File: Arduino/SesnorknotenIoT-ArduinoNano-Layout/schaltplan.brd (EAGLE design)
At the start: 68.2 x 69.8 mm, 10 parts

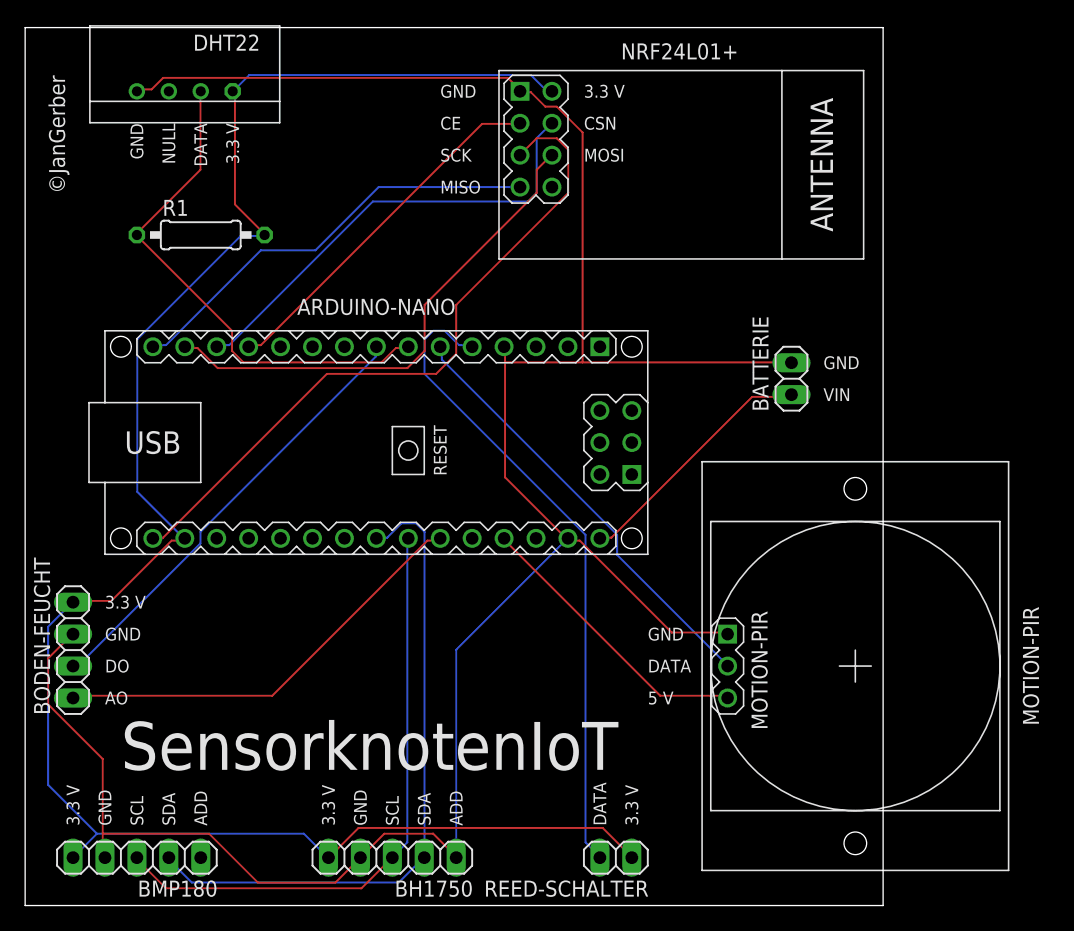
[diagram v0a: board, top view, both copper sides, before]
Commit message: Eagle +Reed Schalter +1-Wire +Schalter stromversorgung
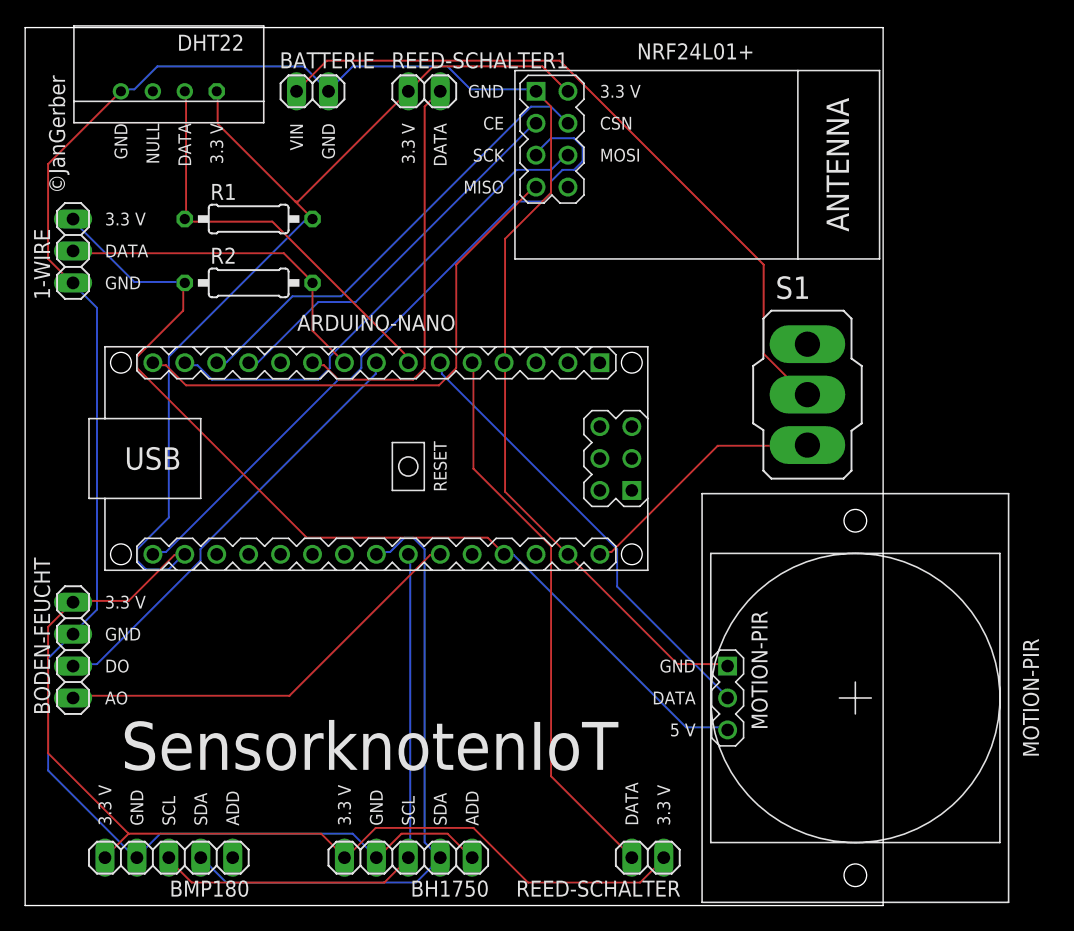
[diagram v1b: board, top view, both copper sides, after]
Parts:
- added 1-WIRE: (no value), pinhead:1X03
- added R2: 4k7, resistor:0207/10
- added REED-SCHALTER1: (no value), pinhead:1X02
- added S1: (no value), switch:320-916
- moved BATTERIE 44.4 mm to (22.9, 64.8), turned to 0 degrees
- moved R1 4.02 mm to (17.8, 54.6)
- moved BMP180 2.54 mm to (11.4, 3.81)
- moved MOTION-PIR 2.54 mm to (66.0, 16.5)
- moved REED-SCHALTER 2.54 mm to (49.5, 3.81)
- moved NRF24L01+ 1.27 mm to (53.3, 58.4)
- moved BH1750 1.27 mm to (30.5, 3.81)
- moved DHT22 1.27 mm to (11.4, 64.8)
- moved ARDUINO-NANO 1.27 mm to (27.9, 35.6)
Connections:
- new net N$5: BATTERIE.1, S1.2
- new net N$6: 1-WIRE.2, ARDUINO-NANO.J1.9, R2.2
- new net N$7: ARDUINO-NANO.J1.10, REED-SCHALTER1.2
- net 3.3V: now also REED-SCHALTER1.1
- net 5V: now also 1-WIRE.3, R2.1
- net GND: now also 1-WIRE.1
- net N$13: now also S1.3; no longer BATTERIE.1
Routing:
- net N$5: track 0.00 -> 57.0 mm
- net 5V: track 23.1 -> 78.3 mm
- net N$7: track 0.00 -> 32.5 mm
- net N$6: track 0.00 -> 27.6 mm
- net 3.3V: track 149.9 -> 160.2 mm
- net MISO: track 34.5 -> 42.6 mm
- net N$1: track 40.8 -> 33.1 mm
- net N$2: track 51.6 -> 44.6 mm
- net SCL: track 48.3 -> 45.1 mm
- net SDA: track 52.6 -> 50.5 mm
- net N$9: track 29.0 -> 30.7 mm
- net N$8: track 34.9 -> 36.1 mm
- net MOSI: track 40.1 -> 39.0 mm
- net SCK: track 54.9 -> 54.0 mm
- net GND: track 194.0 -> 193.1 mm
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
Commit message: Änderungen Sender Verschlüsselung und Encodierung
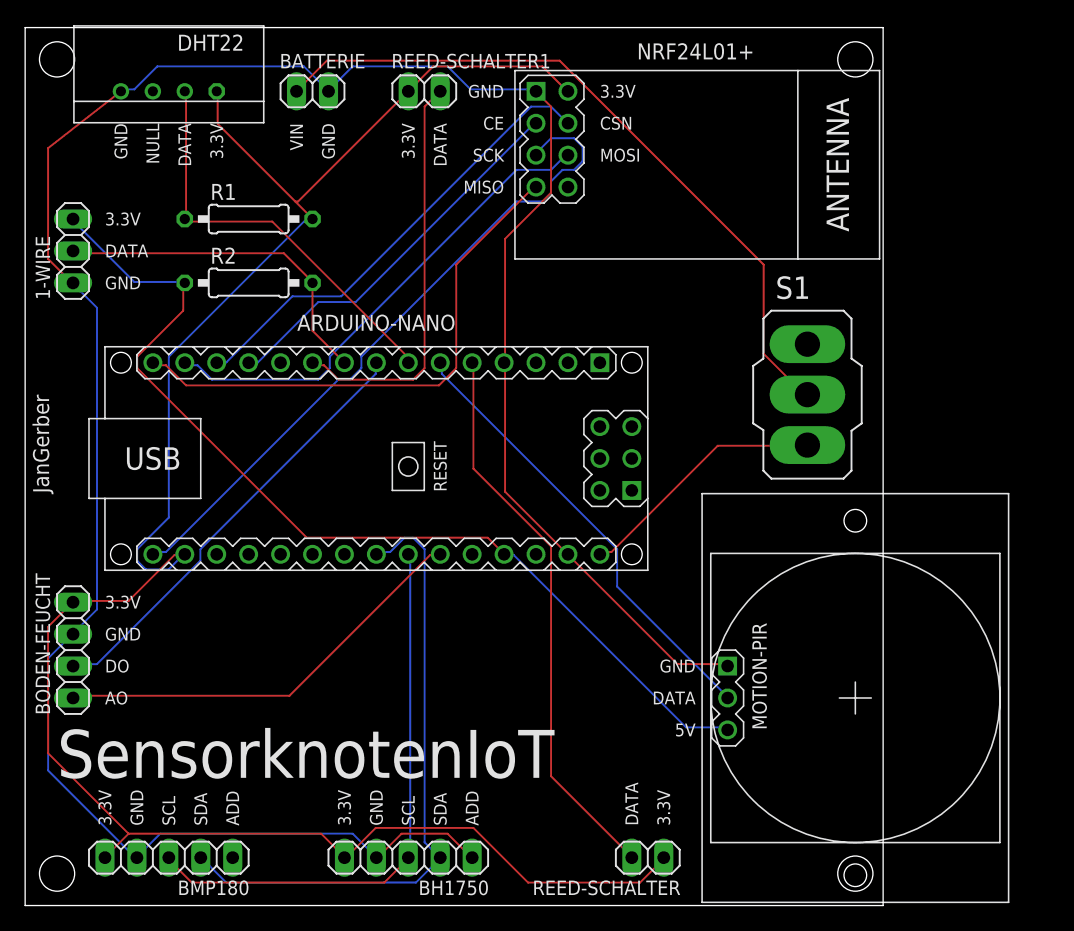
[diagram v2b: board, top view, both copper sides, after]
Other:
- board text added: "3.3V"
- board text added: "5V"
- board text added: "JanGerber"
- board text removed: "3.3 V"
- board text removed: "5 V"
- board text removed: "©JanGerber"
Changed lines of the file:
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@@
 <drawing>
 <settings>
-<setting alwaysvectorfont="no"/>
+<setting alwaysvectorfont="yes"/>
 <setting verticaltext="up"/>
 </settings>
@@
 <text x="53.34" y="19.05" size="1.016" layer="21" rot="R180" align="center-left">GND</text>
 <text x="53.34" y="16.51" size="1.016" layer="21" rot="R180" align="center-left">DATA</text>
-<text x="53.34" y="13.97" size="1.016" layer="21" rot="R180" align="center-left">5 V</text>
-<text x="50.8" y="6.35" size="1.016" layer="21" rot="R90" align="center-left">3.3 V</text>
-<text x="25.4" y="6.35" size="1.016" layer="21" rot="R90" align="center-left">3.3 V</text>
-<text x="6.35" y="6.35" size="1.016" layer="21" rot="R90" align="center-left">3.3 V</text>
-<text x="6.35" y="24.13" size="1.016" layer="21" align="center-left">3.3 V</text>
+<text x="53.34" y="13.97" size="1.016" layer="21" rot="R180" align="center-left">5V</text>
+<text x="50.8" y="6.35" size="1.016" layer="21" rot="R90" align="center-left">3.3V</text>
+<text x="25.4" y="6.35" size="1.016" layer="21" rot="R90" align="center-left">3.3V</text>
+<text x="6.35" y="6.35" size="1.016" layer="21" rot="R90" align="center-left">3.3V</text>
+<text x="6.35" y="24.13" size="1.016" layer="21" align="center-left">3.3V</text>
 <text x="27.94" y="6.35" size="1.016" layer="21" rot="R90" align="center-left">GND</text>
 <text x="8.89" y="6.35" size="1.016" layer="21" rot="R90" align="center-left">GND</text>
@@
 <text x="7.62" y="62.23" size="1.016" layer="21" rot="R270" align="center-left">GND</text>
 <text x="12.7" y="62.23" size="1.016" layer="21" rot="R270" align="center-left">DATA</text>
-<text x="15.24" y="62.23" size="1.016" layer="21" rot="R270" align="center-left">3.3 V</text>
+<text x="15.24" y="62.23" size="1.016" layer="21" rot="R270" align="center-left">3.3V</text>
 <text x="10.16" y="62.23" size="1.016" layer="21" rot="R270" align="center-left">NULL</text>
-<text x="45.72" y="64.77" size="1.016" layer="21" align="center-left">3.3 V</text>
+<text x="45.72" y="64.77" size="1.016" layer="21" align="center-left">3.3V</text>
 <text x="38.1" y="64.77" size="1.016" layer="21" rot="R180" align="center-left">GND</text>
 <text x="38.1" y="59.69" size="1.016" layer="21" rot="R180" align="center-left">SCK</text>
@@
 <text x="38.1" y="62.23" size="1.016" layer="21" rot="R180" align="center-left">CE</text>
 <text x="45.72" y="62.23" size="1.016" layer="21" align="center-left">CSN</text>
-<text x="58.42" y="13.97" size="1.27" layer="21" rot="R90" align="center-left">MOTION-PIR</text>
+<text x="58.42" y="13.97" size="1.143" layer="21" font="vector" rot="R90" align="center-left">MOTION-PIR</text>
 <text x="21.59" y="62.23" size="1.016" layer="21" rot="R270" align="center-left">VIN</text>
 <text x="24.13" y="62.23" size="1.016" layer="21" rot="R270" align="center-left">GND</text>
-<text x="7.62" y="12.7" size="3.81" layer="21" ratio="31" align="center-left">SensorknotenIoT</text>
-<text x="46.99" y="12.7" size="3.81" layer="22" ratio="31" rot="MR0" align="center-left">SensorknotenIoT</text>
-<text x="64.77" y="2.54" size="1.6764" layer="22" ratio="31" rot="MR0" align="center-left">©JanGerber</text>
-<text x="2.54" y="66.04" size="1.27" layer="21" ratio="31" rot="R270" align="center-left">©JanGerber</text>
-<text x="30.48" y="62.23" size="1.016" layer="21" rot="R270" align="center-left">3.3 V</text>
+<text x="31.75" y="1.27" size="1.6764" layer="22" font="vector" ratio="12" rot="MR0" align="center-left">JanGerber</text>
+<text x="1.27" y="40.64" size="1.27" layer="21" font="vector" ratio="11" rot="R270" align="center-left">JanGerber</text>
+<text x="30.48" y="62.23" size="1.016" layer="21" rot="R270" align="center-left">3.3V</text>
 <text x="33.02" y="62.23" size="1.016" layer="21" rot="R270" align="center-left">DATA</text>
 <text x="6.35" y="49.53" size="1.016" layer="21" align="center-left">GND</text>
-<text x="6.35" y="54.61" size="1.016" layer="21" align="center-left">3.3 V</text>
+<text x="6.35" y="54.61" size="1.016" layer="21" align="center-left">3.3V</text>
 <text x="6.35" y="52.07" size="1.016" layer="21" align="center-left">DATA</text>
+<text x="2.54" y="10.16" size="3.81" layer="25" font="vector" ratio="14">SensorknotenIoT</text>
+<text x="50.8" y="10.16" size="3.81" layer="26" font="vector" ratio="14" rot="MR0">SensorknotenIoT</text>
+<hole x="2.54" y="2.54" drill="2.8"/>
+<hole x="66.04" y="2.54" drill="2.8"/>
+<hole x="66.04" y="67.31" drill="2.8"/>
+<hole x="2.54" y="67.31" drill="2.8"/>
 </plain>
 <attributes>
@@
 </autorouter>
 <elements>
-<element name="BATTERIE" library="pinhead" package="1X02" value="" x="22.86" y="64.77"/>
-<element name="BMP180" library="pinhead" package="1X05" value="" x="11.43" y="3.81" rot="R180"/>
+<element name="BATTERIE" library="pinhead" package="1X02" value="" x="22.86" y="64.77" smashed="yes">
+<attribute name="NAME" x="20.2438" y="66.5988" size="1.143" layer="25" font="vector" ratio="10"/>
+<attribute name="VALUE" x="20.32" y="61.595" size="1.27" layer="27"/>
+</element>
+<element name="BMP180" library="pinhead" package="1X05" value="" x="11.43" y="3.81" smashed="yes" rot="R180">
+<attribute name="NAME" x="17.8562" y="1.9812" size="1.143" layer="25" font="vector" ratio="10" rot="R180"/>
+<attribute name="VALUE" x="17.78" y="6.985" size="1.27" layer="27" rot="R180"/>
+</element>
 <element name="ARDUINO-NANO" library="diy-modules" package="ARDUINO-NANO-3.0#ISP" value="" x="27.94" y="35.56"/>
 <element name="NRF24L01+" library="diy-modules" package="WIRELESS-NRF24L01" value="" x="53.34" y="58.42"/>
 <element name="R1" library="resistor" package="0207/10" value="10k" x="17.78" y="54.61"/>
-<element name="MOTION-PIR" library="diy-modules" package="MOTION-PIR-DYP-ME003" value="" x="66.04" y="16.51" rot="R270"/>
+<element name="MOTION-PIR" library="diy-modules" package="MOTION-PIR-DYP-ME003" value="" x="66.04" y="16.51" smashed="yes" rot="R270">
+<attribute name="VALUE" x="52.705" y="16.51" size="1.27" layer="27" rot="R270" align="top-center"/>
+</element>
 <element name="DHT22" library="RHT03_DHT-22_AM2302" package="RHT03_DHT-22" value="" x="11.43" y="64.77" rot="R180">
 <attribute name="PROD_ID" value="SEN-10167" x="11.43" y="64.77" size="1.778" layer="27" rot="R180" display="off"/>
 </element>
-<element name="BH1750" library="pinhead" package="1X05" value="" x="30.48" y="3.81" rot="R180"/>
-<element name="REED-SCHALTER" library="pinhead" package="1X02" value="" x="49.53" y="3.81" rot="R180"/>
-<element name="BODEN-FEUCHT" library="pinhead" package="1X04" value="" x="3.81" y="20.32" rot="R90"/>
-<element name="1-WIRE" library="pinhead" package="1X03" value="" x="3.81" y="52.07" rot="R90"/>
+<element name="BH1750" library="pinhead" package="1X05" value="" x="30.48" y="3.81" smashed="yes" rot="R180">
+<attribute name="NAME" x="36.9062" y="1.9812" size="1.143" layer="25" font="vector" ratio="10" rot="R180"/>
+<attribute name="VALUE" x="36.83" y="6.985" size="1.27" layer="27" rot="R180"/>
+</element>
+<element name="REED-SCHALTER" library="pinhead" package="1X02" value="" x="49.53" y="3.81" smashed="yes" rot="R180">
+<attribute name="NAME" x="52.1462" y="1.9812" size="1.143" layer="25" font="vector" ratio="10" rot="R180"/>
+<attribute name="VALUE" x="52.07" y="6.985" size="1.27" layer="27" rot="R180"/>
+</element>
+<element name="BODEN-FEUCHT" library="pinhead" package="1X04" value="" x="3.81" y="20.32" smashed="yes" rot="R90">
+<attribute name="NAME" x="1.9812" y="15.1638" size="1.143" layer="25" font="vector" ratio="10" rot="R90"/>
+<attribute name="VALUE" x="6.985" y="15.24" size="1.27" layer="27" rot="R90"/>
+</element>
+<element name="1-WIRE" library="pinhead" package="1X03" value="" x="3.81" y="52.07" smashed="yes" rot="R90">
+<attribute name="NAME" x="1.9812" y="48.1838" size="1.143" layer="25" font="vector" ratio="10" rot="R90"/>
+<attribute name="VALUE" x="6.985" y="48.26" size="1.27" layer="27" rot="R90"/>
+</element>
 <element name="R2" library="resistor" package="0207/10" value="4k7" x="17.78" y="49.53"/>
 <element name="S1" library="switch" package="320-916" value="" x="62.23" y="40.64"/>
-<element name="REED-SCHALTER1" library="pinhead" package="1X02" value="" x="31.75" y="64.77"/>
+<element name="REED-SCHALTER1" library="pinhead" package="1X02" value="" x="31.75" y="64.77" smashed="yes">
+<attribute name="NAME" x="29.1338" y="66.5988" size="1.143" layer="25" font="vector" ratio="10"/>
+<attribute name="VALUE" x="29.21" y="61.595" size="1.27" layer="27"/>
+</element>
 </elements>
 <signals>
@@
 <wire x1="24.2316" y1="64.9224" x2="24.13" y2="64.77" width="0.1524" layer="16"/>
 <wire x1="1.8288" y1="51.435" x2="3.6576" y2="49.6062" width="0.1524" layer="1"/>
-<wire x1="1.8288" y1="58.9788" x2="1.8288" y2="51.435" width="0.1524" layer="1"/>
-<wire x1="7.62" y1="64.77" x2="1.8288" y2="58.9788" width="0.1524" layer="1"/>
+<wire x1="1.8288" y1="60.2488" x2="1.8288" y2="51.435" width="0.1524" layer="1"/>
+<wire x1="7.62" y1="64.77" x2="1.8288" y2="60.2488" width="0.1524" layer="1"/>
 <wire x1="3.6576" y1="49.6062" x2="3.81" y2="49.53" width="0.1524" layer="1"/>
 <wire x1="38.1762" y1="53.0352" x2="38.1762" y2="43.2054" width="0.1524" layer="1"/>
